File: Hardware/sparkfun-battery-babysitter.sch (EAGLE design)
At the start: 58 parts, among them U1 BQ24075, U2 BQ27441-G1

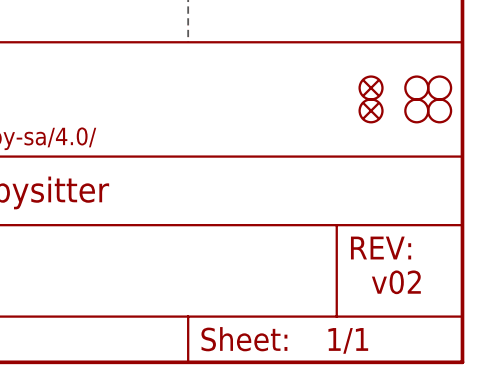
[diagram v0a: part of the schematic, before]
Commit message: Moving some silk, nudging a via, upping to v10
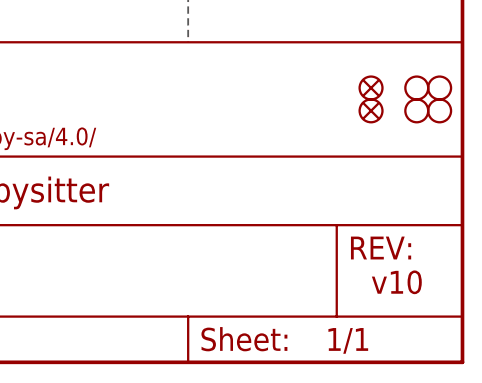
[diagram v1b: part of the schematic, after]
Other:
- note added: "v10"
- note removed: "v02"
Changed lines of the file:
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@@
 <text x="220.98" y="127" size="2.54" layer="94" font="vector" align="top-left">Headers</text>
 <text x="172.72" y="10.16" size="2.54" layer="94" font="vector" align="top-left">Jim Lindblom</text>
-<text x="238.76" y="10.16" size="2.54" layer="94" font="vector" align="top-left">v02</text>
+<text x="238.76" y="10.16" size="2.54" layer="94" font="vector" align="top-left">v10</text>
 <text x="149.86" y="152.4" size="1.27" layer="97" font="vector">SYSOFF controls supply
 to the V_OUT pin.
